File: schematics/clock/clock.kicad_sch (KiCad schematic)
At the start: 25 parts, among them J1 Bus, J2 Bus, SW1 RUN, SW2 PULSE, U1 NE556, U2 74LS27, U3 74LS27

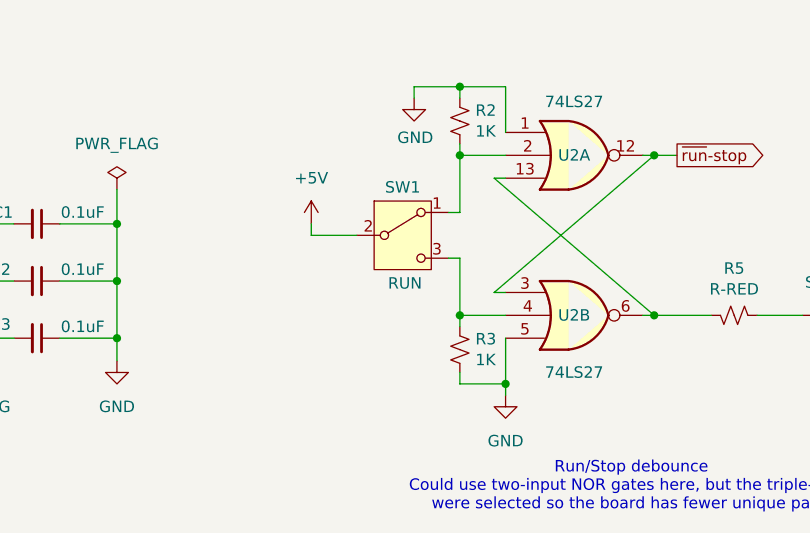
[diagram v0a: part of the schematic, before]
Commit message: swap labels on Clock Module RUN/SSTOP switch
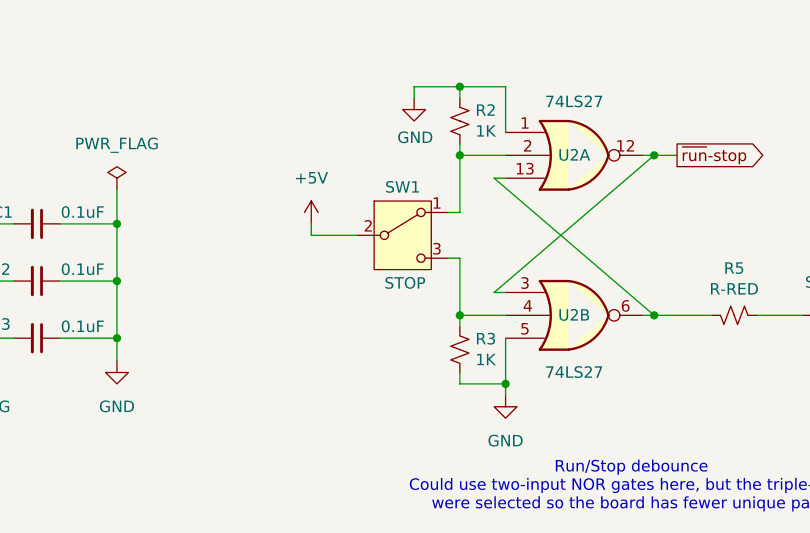
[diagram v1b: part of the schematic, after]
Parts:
- SW1: value RUN -> STOP
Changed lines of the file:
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@@
 			)
 		)
-		(property "Value" "RUN"
+		(property "Value" "STOP"
 			(at 68.834 174.244 0)
 			(effects

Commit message: clock module 2.0 - adds clock divider
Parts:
- removed U2: 74LS27, Package_DIP:DIP-14_W7.62mm, symbol 74xx:74LS27
- added C4: 0.1uF, Capacitor_THT:C_Disc_D3.0mm_W1.6mm_P2.50mm, symbol Device:C_Small
- added C9: 1.5uF, Capacitor_THT:C_Disc_D4.3mm_W1.9mm_P5.00mm, symbol Device:C_Small
- added J3: Conn_02x04_Odd_Even, Connector_PinHeader_2.54mm:PinHeader_2x04_P2.54mm_Vertical, symbol Connector_Generic:Conn_02x04_Odd_Even
- added J4: CLOCK SELECT, Connector_PinHeader_2.54mm:PinHeader_1x03_P2.54mm_Vertical, symbol Connector_Generic:Conn_01x03
- added J5: EXTERNAL CLOCK IN, Connector_PinHeader_2.54mm:PinHeader_1x02_P2.54mm_Vertical, symbol Connector_Generic:Conn_01x02
- added SW3: SPDT, mySwitches:SW_EG1218, symbol Switch:SW_SPDT
- added U2: 74LS02, Package_DIP:DIP-14_W7.62mm, symbol 74xx:74LS02
- added U4: 74LS161, Package_DIP:DIP-16_W7.62mm, symbol 74xx:74LS161
- C8: renamed from C5; value 2.2uF -> 0.047uF; footprint Capacitor_THT:C_Radial_D5.0mm_H5.0mm_P2.00mm -> Capacitor_THT:C_Disc_D4.3mm_W1.9mm_P5.00mm
- RV1: value 1M -> 100K; footprint Potentiometer_THT:Potentiometer_Bourns_3386F_Vertical -> Potentiometer_THT:Potentiometer_Bourns_3386P_Vertical
- SW1: footprint Connector_PinHeader_2.54mm:PinHeader_1x03_P2.54mm_Vertical -> mySwitches:SW_EG1218
- SW2: footprint Button_Switch_THT:SW_PUSH-12mm -> Button_Switch_THT:SW_PUSH-12mm_Wuerth-430476085716
- renumbered C4 to C5
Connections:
- net +5V: now also C4.2, U2.14 (VCC), U4.10 (CET), U4.16 (VCC), U4.3 (D0), U4.4 (D1), U4.5 (D2), U4.6 (D3), U4.7 (CEP), U4.9 (~{PE})
- net GND: now also SW2.2, C4.1, C9.1, J5.2 (Pin_2), U2.5, U2.6, U2.7 (GND), U4.8 (GND); no longer SW2.1
- net astable: now also U3.13, J3.2 (Pin_2), J3.4 (Pin_4), J3.6 (Pin_6), J3.8 (Pin_8); no longer U1.5 (Q), U3.3
- net ~{run}-stop: now also U2.10, U2.11
- net ~{RST}: now reaches J1.3 (Pin_3)
- net ~{RST}: now also U2.2, U2.3
- net at R7.2, U1.8 (TR): now also SW2.1; no longer SW2.2
- net at RV1.2, U1.2 (THR), U1.6 (TR): now also SW3.2 (B); no longer C8.1
- net at R3.1, SW1.3 (C): now also U2.12
- net at R5.1: now also U2.13, U2.9
- net at U3.10, U3.11, U3.12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: now also R6.2; no longer R6.1
- net at U3.6: now also U4.1 (~{MR}); no longer U3.13
- net at R2.2, SW1.1 (A): now also U2.8
- net at D2.1 (K): now also R6.1; no longer R6.2
- new net: C8.1, SW3.3 (C)
- new net: J4.2 (Pin_2), U4.2 (CP)
- new net: C9.2, SW3.1 (A)
- new net DIV16: J3.7 (Pin_7), U4.11 (Q3)
- new net DIV2: J3.1 (Pin_1), U4.14 (Q0)
- new net DIV4: J3.3 (Pin_3), U4.13 (Q1)
- new net DIV8: J3.5 (Pin_5), U4.12 (Q2)
- new net EXT: J4.3 (Pin_3), J5.1 (Pin_1)
- new net INT: J4.1 (Pin_1), U1.5 (Q)
- new net RST: U2.1, U3.3
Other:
- note added: "NOTE: The MR of the clock divider ensures that the clock will always be LOW when coming out of a system reset state. This guarantees that a rising clock pulse will occur during the Microcode T0 step."
- note added: "Run/Stop debounce"
- note added: "clock divider"
- note added: "clock hold"
- note removed: "Run/Stop debounce Could use two-input NOR gates here, but the triple-input were selected so the board has fewer unique parts"
- moved on the sheet: C5, C6, C7, C8, D1, D2, R1, R2, R3, R4, R5, R6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

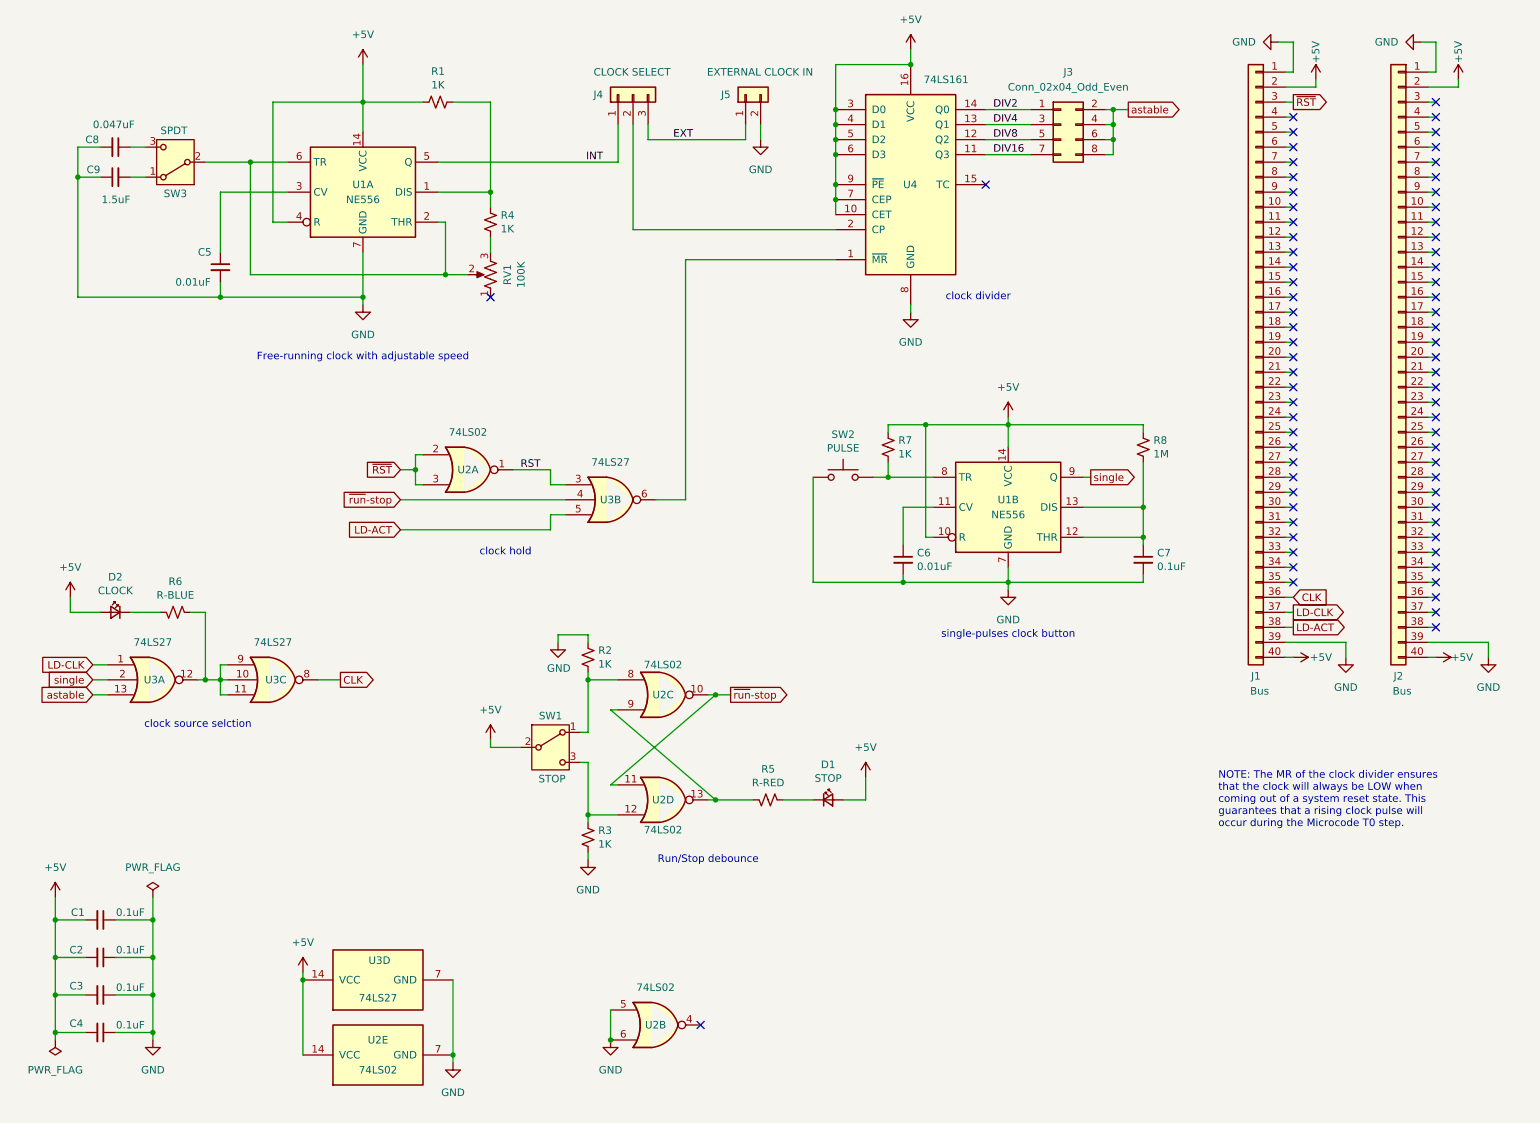
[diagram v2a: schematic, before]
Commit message: document the version 2.0 clock module
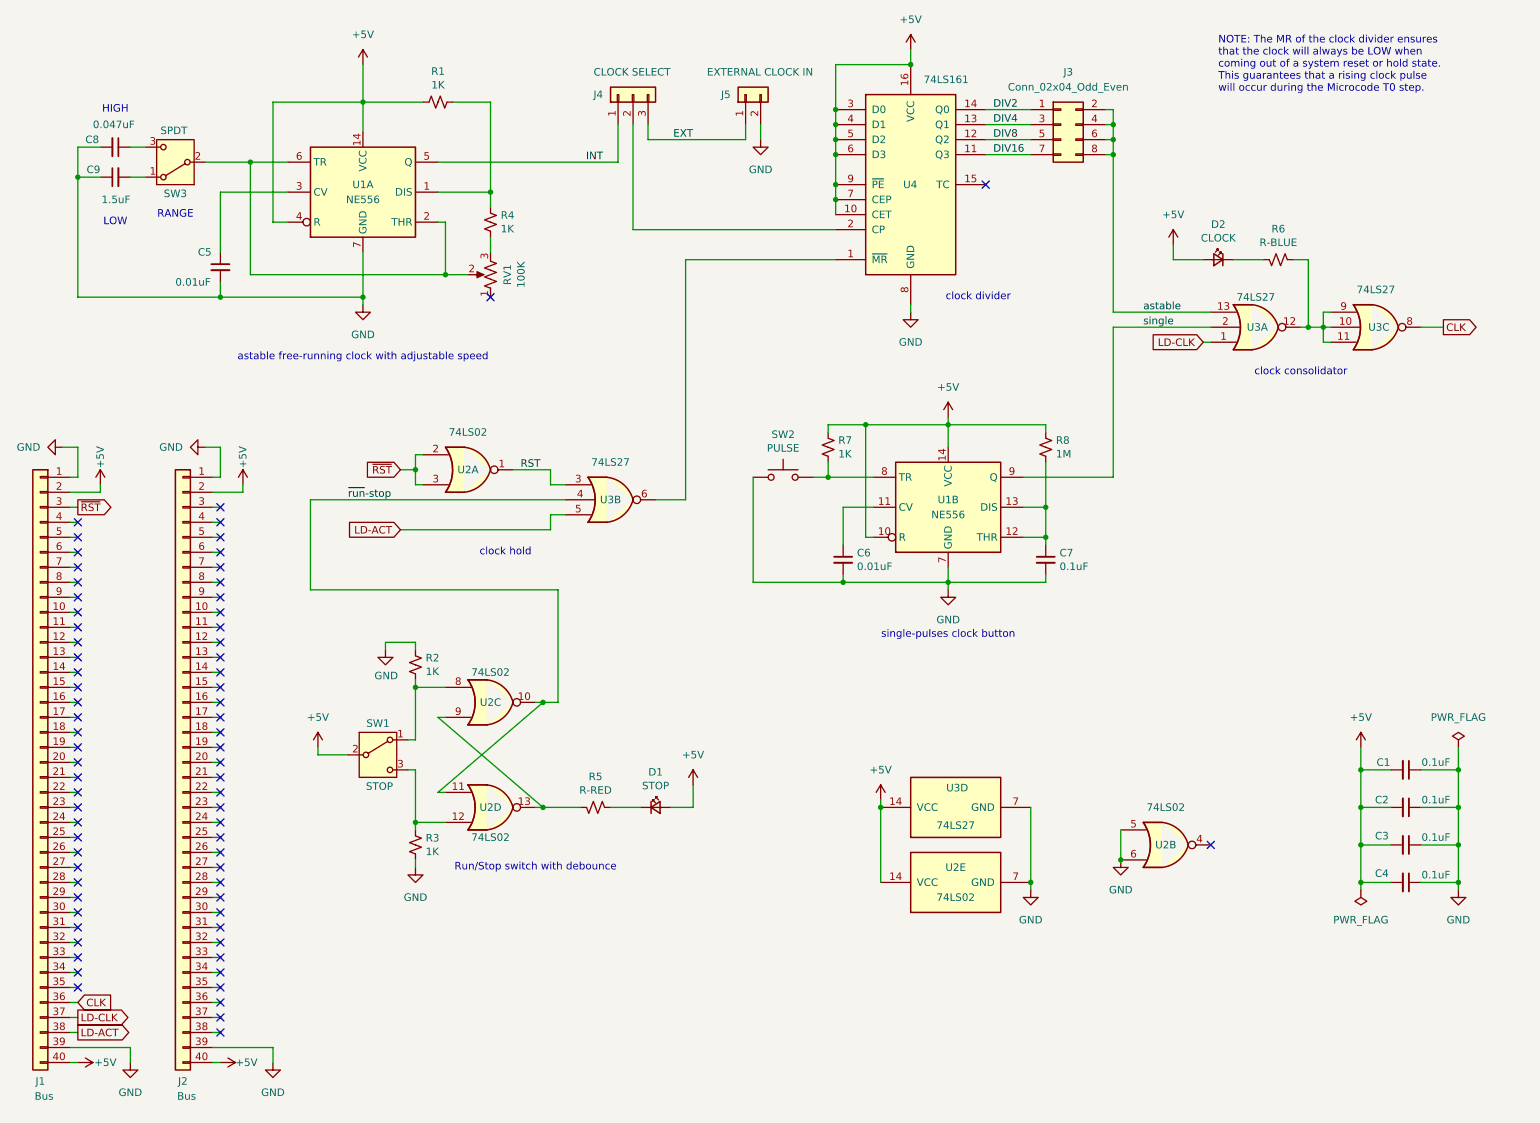
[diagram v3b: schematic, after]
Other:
- note added: "HIGH"
- note added: "LOW"
- note added: "NOTE: The MR of the clock divider ensures that the clock will always be LOW when coming out of a system reset or hold state. This guarantees that a rising clock pulse will occur during the Microcode T0 step."
- note added: "RANGE"
- note added: "Run/Stop switch with debounce"
- note added: "astable free-running clock with adjustable speed"
- note added: "clock consolidator"
- note removed: "Free-running clock with adjustable speed"
- note removed: "NOTE: The MR of the clock divider ensures that the clock will always be LOW when coming out of a system reset state. This guarantees that a rising clock pulse will occur during the Microcode T0 step."
- note removed: "Run/Stop debounce"
- note removed: "clock source selction"
- moved on the sheet: C1, C2, C3, C4, C6, C7, D1, D2, J1, J2, R2, R3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
